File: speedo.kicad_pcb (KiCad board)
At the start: 2 copper layers, 41 parts, among them J1 Conn_01x08, J2 Conn_01x08, Q1 BSS138, U1 A1101ELHL, U2 LT1762, U3 4N25, U4 LT1762, U5 STM32F103C8Tx, Y1 Crystal

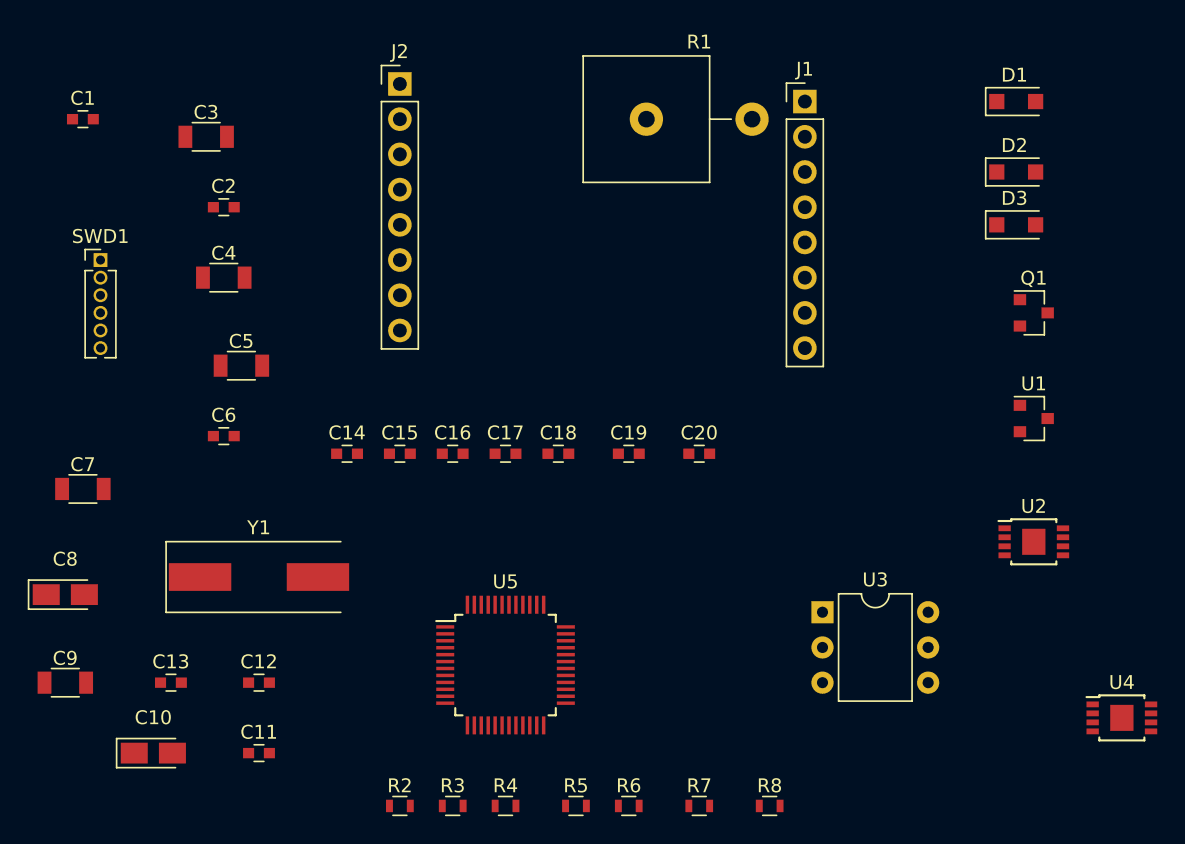
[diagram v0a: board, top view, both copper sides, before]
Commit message: Changed to atmel design
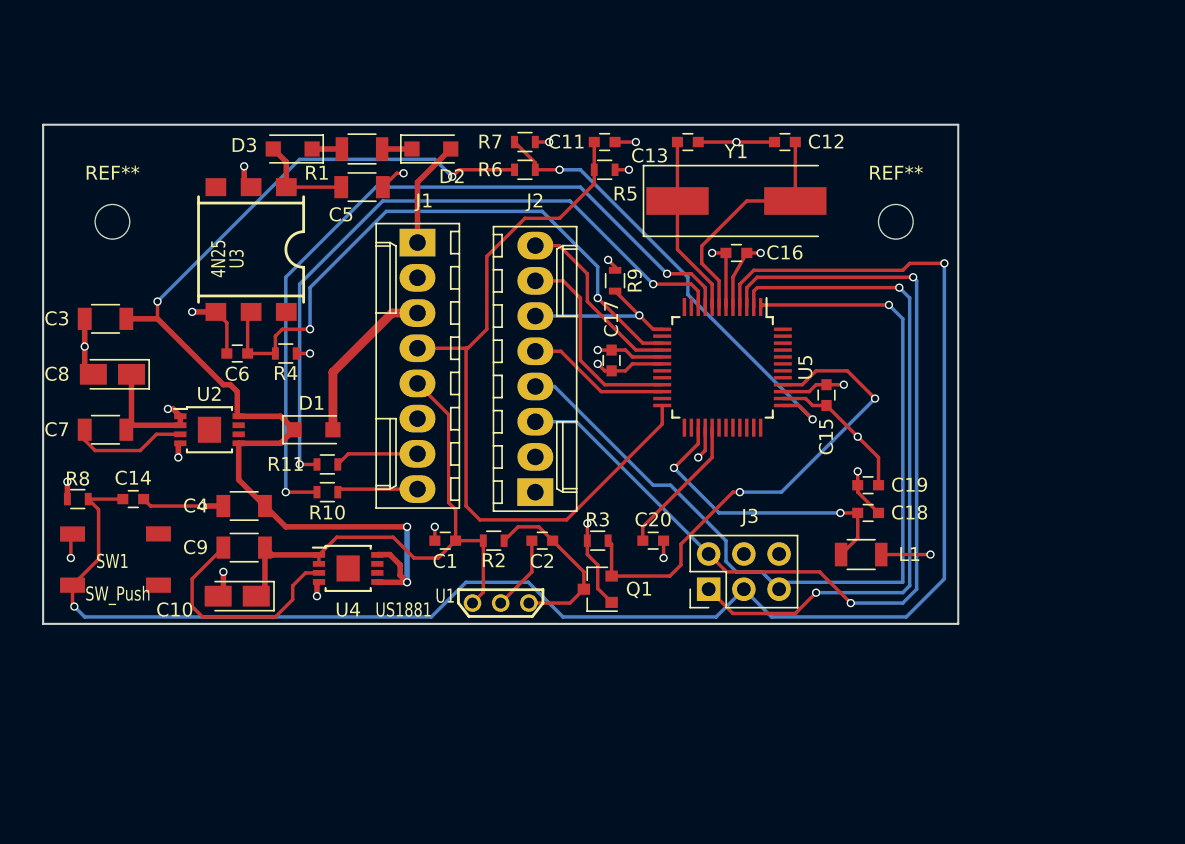
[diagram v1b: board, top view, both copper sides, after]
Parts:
- removed SWD1: Conn_01x06, Pin_Headers:Pin_Header_Straight_1x06_Pitch1.27mm
- added J3: Prog Header, Pin_Headers:Pin_Header_Straight_2x03_Pitch2.54mm, F.Cu at (148.0, 135.5)
- added L1: 10uH, Inductors_SMD:L_1206, F.Cu at (159.0, 133.0)
- added R10: 1K, Resistors_SMD:R_0603, F.Cu at (120.5, 128.5)
- added R11: 1K, Resistors_SMD:R_0603, F.Cu at (120.5, 126.5)
- added R9: 10K, Resistors_SMD:R_0603, F.Cu at (141.2, 113.2)
- added REF**: MountingHole_2.5mm, Mounting_Holes:MountingHole_2.5mm, F.Cu at (105.0, 109.0)
- added REF**: MountingHole_2.5mm, Mounting_Holes:MountingHole_2.5mm, F.Cu at (161.5, 109.0)
- added SW1: SW_Push, custom_footprint:switch-kpt-1187B-SMD, F.Cu at (105.5, 133.5)
- C1: value C -> 100nF
- C11, C6: value C -> 10nF
- C14: value 100nF -> 10nF
- C19: value 100nF -> 10uF
- C2: value C -> 4.7nF
- C5: value C -> 1nF
- J1, J2: footprint Pin_Headers:Pin_Header_Straight_1x08_Pitch2.54mm -> Connectors_Molex:Molex_KK-6410-08_08x2.54mm_Straight
- R1: footprint Resistors_THT:R_Axial_Power_L25.0mm_W9.0mm_P7.62mm_Vertical -> Resistors_SMD:R_1206
- R2, R3, R5, R7: value R -> 10K
- R4: value R -> 4.7K
- R6: value R -> 100K
- U1: value A1101ELHL -> US1881; footprint TO_SOT_Packages_SMD:SOT-23 -> custom_footprint:TO-92-pins-3-in-a-row
- U2: value LT1762 -> LT1762-3.3
- U3: footprint Housings_DIP:DIP-6_W7.62mm -> custom_footprint:4N2X
- U4: value LT1762 -> LT1762-5
- U5: value STM32F103C8Tx -> ATMEGA644-20AU
- Y1: value Crystal -> 10MHz 18pF
- moved U2 60.0 mm to (112.0, 124.0)
- moved U4 56.8 mm to (122.0, 134.0)
- moved D1 55.9 mm to (119.5, 124.0)
- moved R8 54.6 mm to (102.5, 129.0)
- moved C12 54.4 mm to (153.5, 103.2)
- moved C13 53.9 mm to (146.5, 103.2), turned to 180 degrees
- moved D3 52.5 mm to (118.0, 103.8), turned to 180 degrees
- moved C11 50.6 mm to (140.5, 103.2)
- moved R7 49.5 mm to (134.8, 103.2), turned to 180 degrees
- moved U3 48.8 mm to (115.0, 111.0), turned to 270 degrees
- moved R6 46.5 mm to (134.8, 105.2), turned to 180 degrees
- moved R5 45.9 mm to (140.5, 105.2), turned to 180 degrees
- moved Y1 43.8 mm to (150.0, 107.5)
- moved D2 42.2 mm to (128.0, 103.8)
- moved U1 40.7 mm to (133.0, 136.5)
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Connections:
- C14 pad 1: NRST -> Reset
- C15 pad 1: GND -> +3V3
- C15 pad 2: +3V3 -> GND
- C16 pad 1: GND -> +3V3
- C16 pad 2: +3V3 -> GND
- C17 pad 1: GND -> +3V3
- C17 pad 2: +3V3 -> GND
- C18 pad 1: GND -> Net-(C18-Pad1)
- C18 pad 2: +3V3 -> GND
- C19 pad 1: GND -> +3V3
- C19 pad 2: +3V3 -> GND
- C2 pad 1: GND -> Net-(C2-Pad1)
- C2 pad 2: Net-(C2-Pad2) -> GND
- C20 pad 1: GND -> Net-(C20-Pad1)
- C20 pad 2: +3V3 -> GND
- C3 pad 1: Net-(C3-Pad1) -> VIN
- C4 pad 1: Net-(C3-Pad1) -> VIN
- D1 pad 1: Net-(C3-Pad1) -> VIN
- D1 pad 2: VIN -> +12V
- J2 pad 3: VIN -> +12V
- J2 pad 7: Net-(J2-Pad7) -> TX
- J2 pad 8: Net-(J2-Pad8) -> RX
- Q1 pad 3: Net-(C2-Pad2) -> Net-(C2-Pad1)
- R2 pad 1: Net-(C2-Pad2) -> Net-(C2-Pad1)
- R8 pad 1: BOOT0 -> +3V3
- R8 pad 2: GND -> Reset
- U1 pad 3: Net-(C2-Pad2) -> Net-(C2-Pad1)
- U2 pad 5: Net-(C3-Pad1) -> VIN
- U2 pad 8: Net-(C3-Pad1) -> VIN
- U4 pad 5: Net-(C3-Pad1) -> VIN
- U4 pad 8: Net-(C3-Pad1) -> VIN
- U5 pad 1: Net-(U5-Pad1) -> MOSI
- U5 pad 10: LCD-DC -> Net-(R11-Pad2)
- U5 pad 11: LCD-RST -> Net-(U5-Pad11)
- U5 pad 13: Net-(U5-Pad13) -> LCD-CS
- U5 pad 15: VMEAS -> TACH
- U5 pad 16: Net-(U5-Pad16) -> LCD-LED
- U5 pad 17: Net-(U5-Pad17) -> +3V3
- U5 pad 18: Net-(U5-Pad18) -> GND
- U5 pad 2: COIL -> MISO
- U5 pad 21: Net-(U5-Pad21) -> LCD-RST
- U5 pad 22: Net-(U5-Pad22) -> LCD-DC
- U5 pad 23: GND -> Net-(U5-Pad23)
- U5 pad 24: +3V3 -> BUTTON
- U5 pad 25: LCD-CS -> Net-(U5-Pad25)
- U5 pad 26: SCK -> Net-(U5-Pad26)
- U5 pad 27: Net-(U5-Pad27) -> Net-(C18-Pad1)
- U5 pad 28: MOSI -> GND
- U5 pad 29: Net-(U5-Pad29) -> Net-(C20-Pad1)
- U5 pad 3: Net-(U5-Pad3) -> SCK
- U5 pad 32: LCD-LED -> Net-(U5-Pad32)
- U5 pad 34: SWDIO -> Net-(U5-Pad34)
- U5 pad 35: GND -> Net-(U5-Pad35)
- U5 pad 36: +3V3 -> Net-(U5-Pad36)
- U5 pad 37: SWCLK -> VMEAS
- U5 pad 38: Net-(U5-Pad38) -> +3V3
- U5 pad 39: SWO -> GND
- U5 pad 4: BUTTON -> Reset
- U5 pad 41: TACH -> Net-(U5-Pad41)
- U5 pad 44: BOOT0 -> Net-(U5-Pad44)
- U5 pad 45: Net-(U5-Pad45) -> (no net)
- U5 pad 46: Net-(U5-Pad46) -> (no net)
- U5 pad 47: GND -> (no net)
- U5 pad 48: +3V3 -> (no net)
- U5 pad 5: Net-(C12-Pad2) -> +3V3
- U5 pad 6: Net-(C13-Pad2) -> GND
- U5 pad 7: NRST -> Net-(C12-Pad2)
- U5 pad 8: GND -> Net-(C13-Pad2)
- U5 pad 9: +3V3 -> Net-(R10-Pad2)
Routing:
- net Reset: track 0.00 -> 119.1 mm, vias 0 -> 2
- net VIN: track 0.00 -> 78.5 mm, vias 0 -> 4
- net SCK: track 0.00 -> 69.6 mm, vias 0 -> 2
- net MOSI: track 0.00 -> 63.4 mm, vias 0 -> 1
- net GND: track 0.00 -> 61.0 mm, vias 0 -> 19
- net Net-(R10-Pad2): track 0.00 -> 55.1 mm, vias 0 -> 2
- net BUTTON: track 0.00 -> 54.1 mm
- net MISO: track 0.00 -> 49.6 mm, vias 0 -> 2
- net Net-(R11-Pad2): track 0.00 -> 49.3 mm, vias 0 -> 2
- net TACH: track 0.00 -> 45.0 mm, vias 0 -> 2
- net +3V3: track 0.00 -> 44.8 mm, vias 0 -> 10
- net +5V: track 0.00 -> 39.3 mm
- net HALL-EFF: track 0.00 -> 35.7 mm, vias 0 -> 2
- net VMEAS: track 0.00 -> 33.4 mm, vias 0 -> 2
- net Net-(C18-Pad1): track 0.00 -> 21.7 mm, vias 0 -> 2
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- added copper zone on In2.Cu, net +3V3
- added copper zone on In1.Cu, net GND
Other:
- board outline added: 66 x 36 mm
- copper layers 2 -> 4
- net class power added: clearance 0.25, trace_width 0.64, via_dia 1.5, via_drill 0.9
- net class signal added: clearance 0.16, trace_width 0.18, via_dia 0.65, via_drill 0.35
- rule trace_min: 0.2 -> 0.127
- rule via_min_drill: 0.3 -> 0.254
- rule via_min_size: 0.4 -> 0.46

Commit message: Removed traces, redid placement
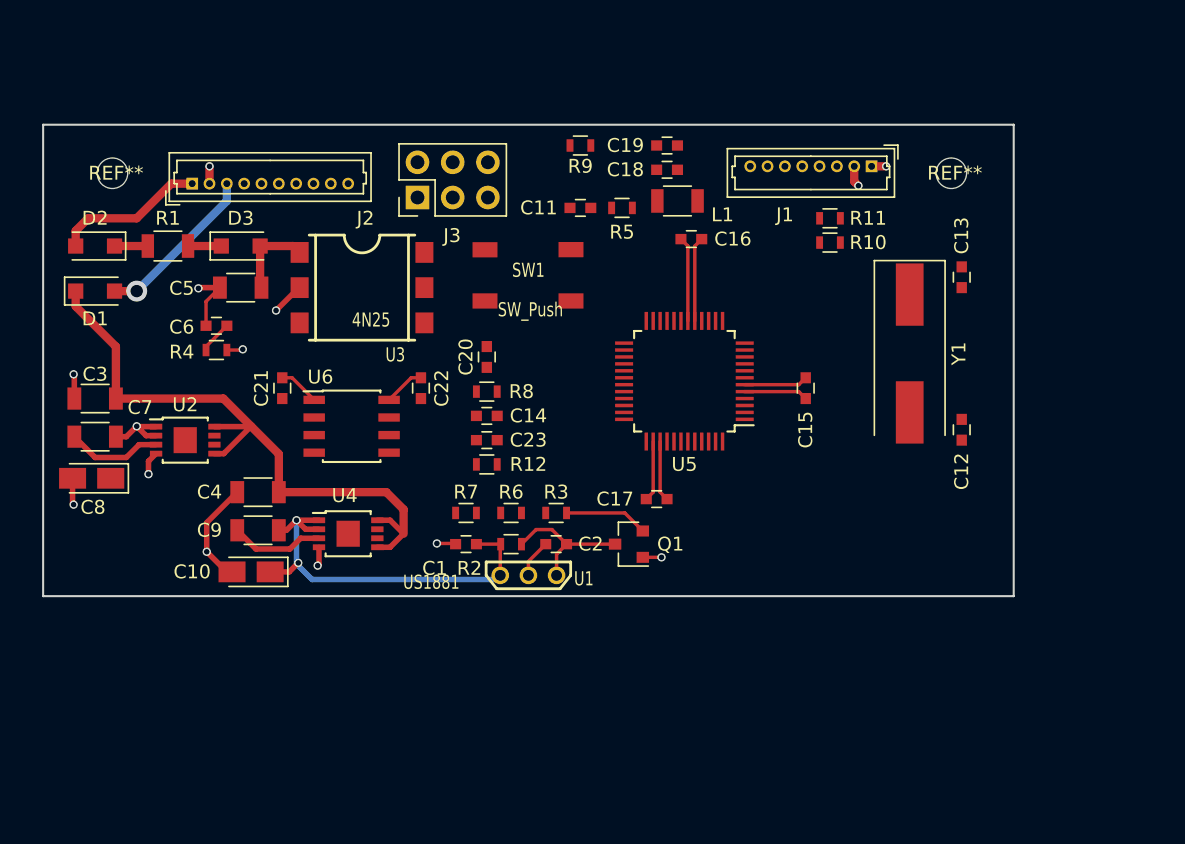
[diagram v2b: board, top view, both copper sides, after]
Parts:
- removed the REF** at (105.0, 109.0)
- removed the REF** at (161.5, 109.0)
- added C21: 100nF, Capacitors_SMD:C_0603, F.Cu at (117.2, 121.0)
- added C22: 100nF, Capacitors_SMD:C_0603, F.Cu at (127.2, 121.0)
- added C23: 10nF, Capacitors_SMD:C_0603, F.Cu at (132.0, 124.8)
- added R12: 10K, Resistors_SMD:R_0603, F.Cu at (132.0, 126.5)
- added REF**: MountingHole_2.2mm_M2, Mounting_Holes:MountingHole_2.2mm_M2, F.Cu at (165.5, 105.5)
- added REF**: MountingHole_2.2mm_M2, Mounting_Holes:MountingHole_2.2mm_M2, F.Cu at (105.0, 105.5)
- added U6: ADuM1200BR, Housings_SOIC:SOIC-8_3.9x4.9mm_Pitch1.27mm, F.Cu at (122.2, 123.8)
- J1: footprint Connectors_Molex:Molex_KK-6410-08_08x2.54mm_Straight -> Connectors_Molex:Molex_PicoBlade_53047-0810_08x1.25mm_Straight
- J2: value Conn_01x08 -> Conn_01x10; footprint Connectors_Molex:Molex_KK-6410-08_08x2.54mm_Straight -> Connectors_Molex:Molex_PicoBlade_53047-1010_10x1.25mm_Straight
- moved R10 40.5 mm to (156.8, 110.5)
- moved R11 40.4 mm to (156.8, 108.8)
- moved SW1 36.1 mm to (135.2, 113.0)
- moved J3 35.2 mm to (127.0, 107.2)
- moved J1 33.8 mm to (159.8, 105.0), turned to 180 degrees
- moved R8 30.5 mm to (132.0, 121.2)
- moved L1 28.7 mm to (145.8, 107.5)
- moved C18 28.7 mm to (145.0, 105.2)
- moved C19 28.5 mm to (145.0, 103.5)
- moved R7 27.1 mm to (130.5, 130.0)
- moved C14 26.2 mm to (132.0, 123.0)
- moved D2 25.2 mm to (103.8, 110.8), turned to 180 degrees
- moved R6 24.8 mm to (133.8, 130.0)
- moved C12 24.4 mm to (166.2, 124.0), turned to 270 degrees
- moved C13 22.0 mm to (166.2, 113.0), turned to 90 degrees
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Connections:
- C11 pad 1: BUTTON -> BUTTON1
- J2 pad 4: BUTTON -> +5V
- J2 pad 5: +5V -> BUTTON1
- J2 pad 6: Net-(J2-Pad6) -> BUTTON2
- J2 pad 7: TX -> GPIO1
- J2 pad 8: RX -> GPIO2
- R5 pad 2: BUTTON -> BUTTON1
- U5 pad 24: BUTTON -> BUTTON1
- U5 pad 25: Net-(U5-Pad25) -> BUTTON2
- U5 pad 30: Net-(U5-Pad30) -> GPIO1-ISO
- U5 pad 31: Net-(U5-Pad31) -> GPIO2-ISO
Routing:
- net Reset: track 119.1 -> 0.00 mm, vias 2 -> 0
- net SCK: track 69.6 -> 0.00 mm, vias 2 -> 0
- net MOSI: track 63.4 -> 0.00 mm, vias 1 -> 0
- net Net-(R10-Pad2): track 55.1 -> 0.00 mm, vias 2 -> 0
- net BUTTON: track 54.1 -> 0.00 mm
- net MISO: track 49.6 -> 0.00 mm, vias 2 -> 0
- net Net-(R11-Pad2): track 49.3 -> 0.00 mm, vias 2 -> 0
- net TACH: track 45.0 -> 2.37 mm, vias 2 -> 0
- net VMEAS: track 33.4 -> 0.00 mm, vias 2 -> 0
- net VIN: track 78.5 -> 47.1 mm, vias 4 -> 0
- net HALL-EFF: track 35.7 -> 6.04 mm, vias 2 -> 0
- net Net-(C18-Pad1): track 21.7 -> 0.00 mm, vias 2 -> 0
- net GND: track 61.0 -> 43.0 mm, vias 19 -> 10
- net +3V3: track 44.8 -> 27.5 mm, vias 10 -> 4
- net Net-(C12-Pad2): track 17.3 -> 0.00 mm
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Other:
- board size 66 x 36 mm -> 70 x 34 mm

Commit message: changed atmega644 to atmega328
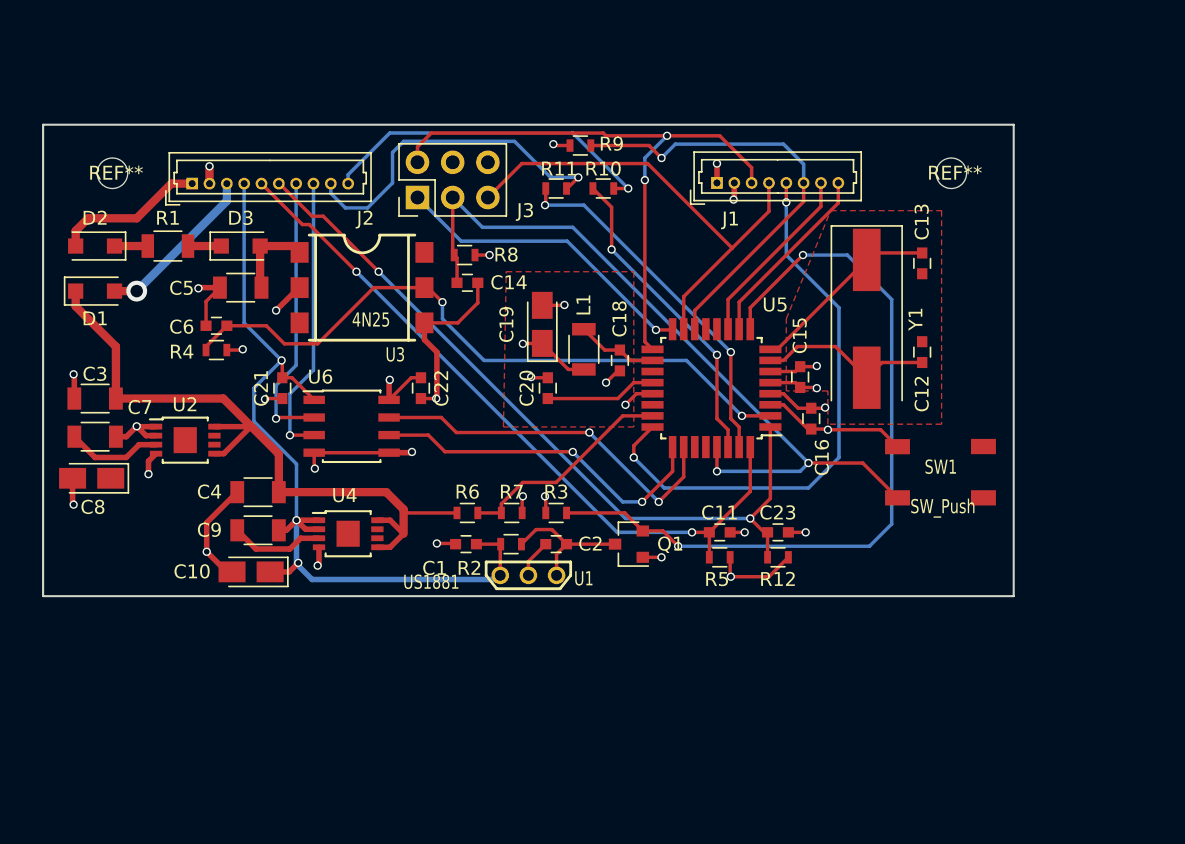
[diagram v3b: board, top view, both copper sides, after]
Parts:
- removed C17: 100nF, Capacitors_SMD:C_0603
- C19: footprint Capacitors_SMD:C_0603 -> Capacitors_Tantalum_SMD:CP_Tantalum_Case-A_EIA-3216-18_Reflow
- U5: value ATMEGA644-20AU -> ATMEGA328P-AU; footprint Housings_QFP:LQFP-48_7x7mm_Pitch0.5mm -> Housings_QFP:TQFP-32_7x7mm_Pitch0.8mm
- moved SW1 33.0 mm to (165.0, 127.2)
- moved R5 26.2 mm to (148.8, 133.2)
- moved C11 25.5 mm to (148.8, 131.4)
- moved R12 22.0 mm to (153.0, 133.2), turned to 180 degrees
- moved C23 22.0 mm to (153.0, 131.4)
- moved R11 19.9 mm to (137.0, 106.6)
- moved R10 16.8 mm to (140.4, 106.6)
- moved C19 15.7 mm to (136.0, 116.4), turned to 90 degrees
- moved C16 15.6 mm to (155.4, 123.2), turned to 270 degrees
- moved C18 14.2 mm to (141.6, 119.0), turned to 270 degrees
- moved L1 12.7 mm to (139.0, 118.2), turned to 270 degrees
- moved J1 11.2 mm to (148.6, 106.2), turned to 0 degrees
- moved R8 9.98 mm to (130.4, 111.4), turned to 180 degrees
- moved C14 9.70 mm to (130.6, 113.4)
- moved C12 6.28 mm to (163.4, 118.4)
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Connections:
- net Net-(C12-Pad2) renamed /xtal1
- net Net-(C13-Pad2) renamed /xtal2
- J3 pad 6: +3V3 -> Net-(J3-Pad6)
- L1 pad 1: +3V3 -> Net-(C18-Pad1)
- L1 pad 2: Net-(C18-Pad1) -> +3V3
- U5 pad 1: MOSI -> BUTTON2
- U5 pad 10: Net-(R11-Pad2) -> LCD-LED
- U5 pad 11: Net-(U5-Pad11) -> LCD-RST
- U5 pad 13: LCD-CS -> Net-(U5-Pad13)
- U5 pad 14: Net-(U5-Pad14) -> LCD-CS
- U5 pad 15: TACH -> MOSI
- U5 pad 16: LCD-LED -> MISO
- U5 pad 17: +3V3 -> SCK
- U5 pad 18: GND -> Net-(C18-Pad1)
- U5 pad 2: MISO -> TACH
- U5 pad 20: Net-(U5-Pad20) -> Net-(C20-Pad1)
- U5 pad 21: LCD-RST -> GND
- U5 pad 22: LCD-DC -> Net-(U5-Pad22)
- U5 pad 23: Net-(U5-Pad23) -> VMEAS
- U5 pad 24: BUTTON1 -> LCD-DC
- U5 pad 25: BUTTON2 -> GPIO2-ISO
- U5 pad 26: Net-(U5-Pad26) -> GPIO1-ISO
- U5 pad 27: Net-(C18-Pad1) -> Net-(U5-Pad27)
- U5 pad 28: GND -> Net-(U5-Pad28)
- U5 pad 29: Net-(C20-Pad1) -> Reset
- U5 pad 3: SCK -> GND
- U5 pad 30: GPIO1-ISO -> Net-(R10-Pad2)
- U5 pad 31: GPIO2-ISO -> Net-(R11-Pad2)
- U5 pad 32: Net-(U5-Pad32) -> BUTTON1
- U5 pad 4: Reset -> +3V3
- U5 pad 5: +3V3 -> GND
- U5 pad 6: GND -> +3V3
- U5 pad 9: Net-(R10-Pad2) -> HALL-EFF
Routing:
- net Reset: track 0.00 -> 56.1 mm, vias 0 -> 2
- net BUTTON2: track 0.00 -> 54.7 mm, vias 0 -> 2
- net BUTTON1: track 0.00 -> 51.9 mm, vias 0 -> 2
- net HALL-EFF: track 6.04 -> 56.0 mm, vias 0 -> 2
- net TACH: track 2.37 -> 48.3 mm, vias 0 -> 2
- net SCK: track 0.00 -> 44.1 mm, vias 0 -> 2
- net LCD-DC: track 0.00 -> 40.8 mm, vias 0 -> 2
- net MOSI: track 0.00 -> 34.3 mm
- net LCD-CS: track 0.00 -> 32.0 mm, vias 0 -> 1
- net GND: track 43.0 -> 74.7 mm, vias 10 -> 23
- net +5V: track 33.0 -> 61.7 mm, vias 2 -> 3
- net GPIO1-ISO: track 0.00 -> 26.8 mm, vias 0 -> 2
- net Net-(R11-Pad2): track 0.00 -> 26.1 mm, vias 0 -> 2
- net GPIO2-ISO: track 0.00 -> 25.1 mm, vias 0 -> 2
- net RX: track 0.00 -> 24.8 mm, vias 0 -> 1
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- added copper zone on F.Cu, net GND
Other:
- board text added: "www.bit-builder.com speedo - v2.0"

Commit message: Fixed footprints
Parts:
- J1: footprint Connectors_Molex:Molex_PicoBlade_53047-0810_08x1.25mm_Straight -> Connectors_Molex:Molex_PicoBlade_53398-0871_08x1.25mm_Straight
- J2: footprint Connectors_Molex:Molex_PicoBlade_53047-1010_10x1.25mm_Straight -> Connectors_Molex:Molex_PicoBlade_53398-1071_10x1.25mm_Straight
- U2, U4: footprint Housings_SSOP:MSOP-8-1EP_3x3mm_Pitch0.65mm -> Housings_SSOP:MSOP-8_3x3mm_Pitch0.65mm
- moved R9 9.88 mm to (146.6, 109.5), turned to 180 degrees
- moved J2 9.81 mm to (120.5, 105.2)
- moved J3 6.15 mm to (133.1, 108.0)
- moved R11 5.51 mm to (141.8, 103.9)
- moved J1 3.86 mm to (152.3, 105.1)
- moved C3 1.65 mm to (103.7, 120.1)
- moved R10 1.61 mm to (141.8, 105.8)
- moved C8 0.51 mm to (103.6, 128.0)
- moved U2 0.16 mm to (110.1, 124.7)
- moved U4 0.10 mm to (121.9, 131.5)
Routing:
- net GND: track 74.7 -> 85.7 mm, vias 23 -> 22
- net LCD-CS: track 32.0 -> 22.5 mm, vias 1 -> 2
- net +3V3: track 36.5 -> 45.8 mm
- net MOSI: track 34.3 -> 26.9 mm
- net RX: track 24.8 -> 17.8 mm, vias 1 -> 0
- net MISO: track 22.4 -> 16.0 mm
- net COIL: track 10.9 -> 17.3 mm
- net +12V: track 12.0 -> 18.2 mm, vias 1 -> 2
- net BUTTON2: track 54.7 -> 60.7 mm
- net TX: track 24.5 -> 19.3 mm, vias 1 -> 0
- net BUTTON1: track 51.9 -> 56.6 mm
- net Reset: track 56.1 -> 60.4 mm, vias 2 -> 4
- net GPIO2: track 20.6 -> 24.6 mm, vias 1 -> 2
- net +5V: track 61.7 -> 64.8 mm, vias 3 -> 4
- net LCD-DC: track 40.8 -> 43.5 mm
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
